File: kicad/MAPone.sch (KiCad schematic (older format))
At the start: 33 parts, among them J1 BARREL_JACK, J2 USB-Micro, P1 CONN_1, P2 CONN_1, P3 CONN_1, P4 CONN_1, SW1 RST, U1 7805, U2 ATMEGA328-P, X1 16MHz

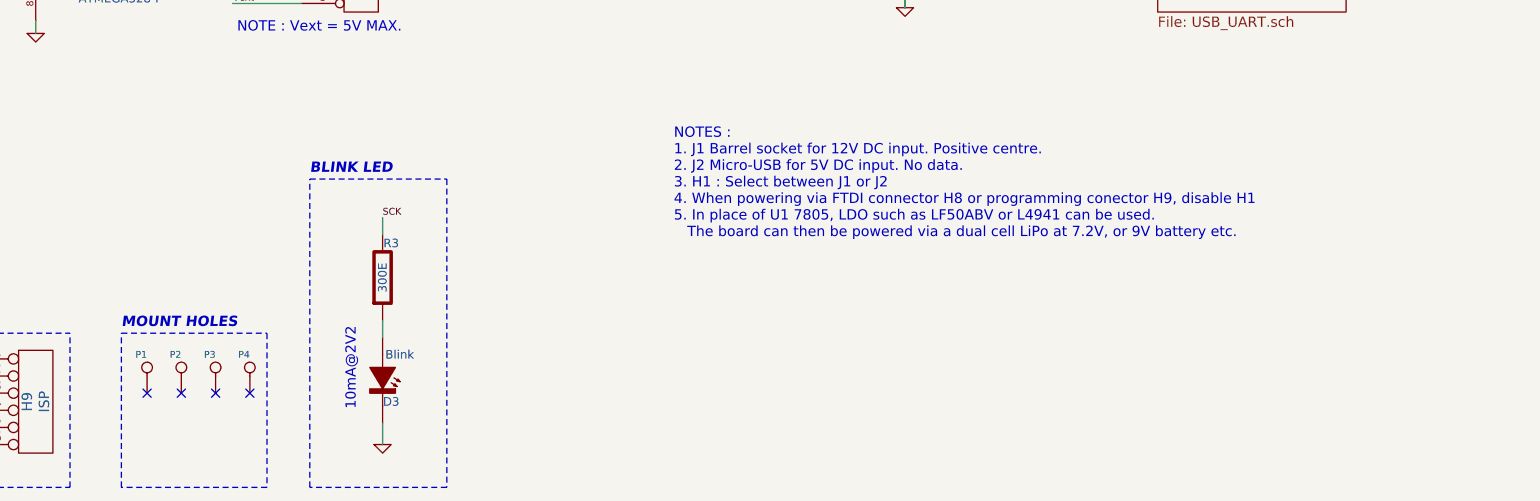
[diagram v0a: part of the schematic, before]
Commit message: MAPone Schematic, PCB, BoM complete. USB<>UART PCB work in progress
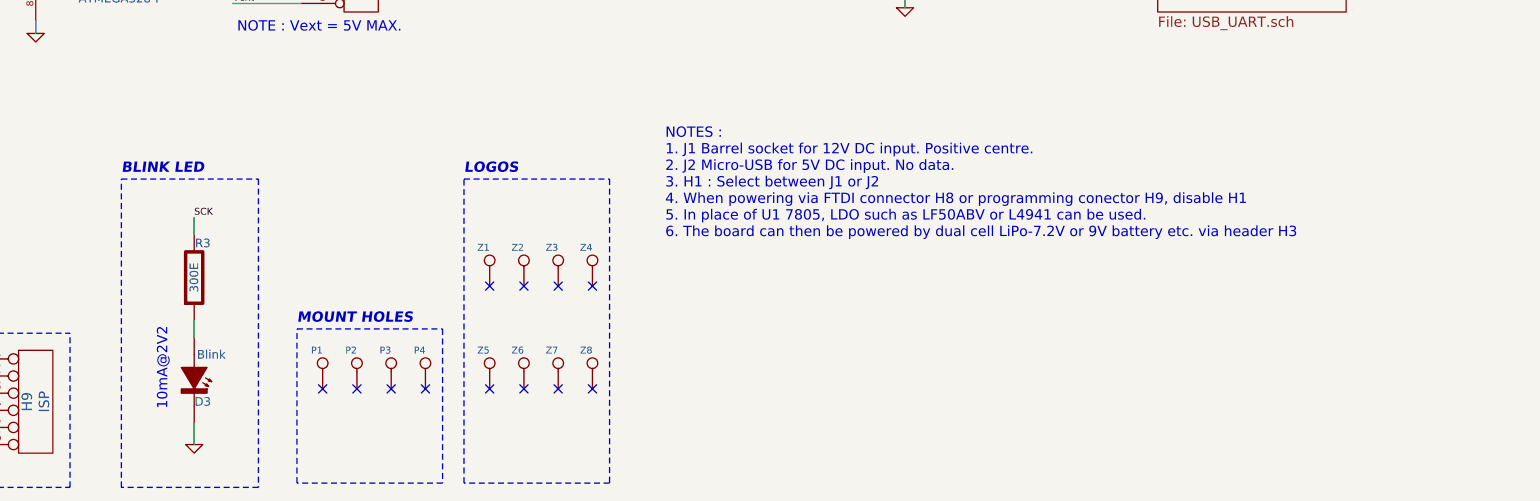
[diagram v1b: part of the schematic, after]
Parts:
- added Z1, Z2, Z3, Z4: CONN_1, MAPone.pretty:MA_Logo2, symbol CONN_1
- added Z5, Z6, Z7, Z8: CONN_1, MAPone:OSHW_6mm, symbol CONN_1
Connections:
- no-connect marks 10 -> 18
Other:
- note added: "LOGOS"
- note added: "NOTES :\n1. J1 Barrel socket for 12V DC input. Positive centre.\n2. J2 Micro-USB for 5V DC input. No data.\n3. H1 : Select between J1 or J2\n4. When powering via FTDI connector H8 or programming conector H9, disable H1\n5. In place of U1 7805, LDO such as LF50ABV or L4941 can be used. \n6. The board can then be powered by dual cell LiPo-7.2V or 9V battery etc. via header H3"
- note removed: "NOTES :\n1. J1 Barrel socket for 12V DC input. Positive centre.\n2. J2 Micro-USB for 5V DC input. No data.\n3. H1 : Select between J1 or J2\n4. When powering via FTDI connector H8 or programming conector H9, disable H1\n5. In place of U1 7805, LDO such as LF50ABV or L4941 can be used. \n The board can then be powered via a dual cell LiPo at 7.2V, or 9V battery etc."
- moved on the sheet: D3, P1, P2, P3, P4, R3
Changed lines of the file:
@@
 00 11 60 41 10 04 41 18 00 44 80 05 41 10 04 61 00 10 01 16 04 41 10 84 01 40 04 58 10 04 41 10
 06 00 11 60 41 10 04 41 18 00 44 80 05 41 10 04 61 00 10 01 16 04 41 10 84 01 E0 7F 01 2F 14 66
-D9 0D DF 91 84 00 00 00 00 49 45 4E 44 AE 42 60 82 48
+D9 0D DF 91 84 00 00 00 00 49 45 4E 44 AE 42 60 82 CE
 EndData
 $EndBitmap
@@
 Connection ~ 1325 2725
 Wire Wire Line
-	5300 7375 5300 7500
-Wire Wire Line
-	5300 6175 5300 6275
+	4200 7375 4200 7500
+Wire Wire Line
+	4200 6175 4200 6275
 Wire Wire Line
 	1050 2725 2375 2725
@@
 	1125 2625 1125 2500
 Wire Wire Line
-	5300 6775 5300 6875
+	4200 6775 4200 6875
 Wire Wire Line
 	10700 1350 10700 1550
@@
 $EndComp
 NoConn ~ 4575 1675
-Text Label 5300 6175 0    40   ~ 0
+Text Label 4200 6175 0    40   ~ 0
 SCK
 $Comp
 L GND #PWR03
 U 1 1 546B82E7
-P 5300 7500
-F 0 "#PWR03" H 5300 7500 30  0001 C CNN
-F 1 "GND" H 5300 7430 30  0001 C CNN
-F 2 "" H 5300 7500 60  0001 C CNN
-F 3 "" H 5300 7500 60  0001 C CNN
-	1    5300 7500
+P 4200 7500
+F 0 "#PWR03" H 4200 7500 30  0001 C CNN
+F 1 "GND" H 4200 7430 30  0001 C CNN
+F 2 "" H 4200 7500 60  0001 C CNN
+F 3 "" H 4200 7500 60  0001 C CNN
+	1    4200 7500
 	1    0    0    -1
 $EndComp
@@
 L R_CPL R3
 U 1 1 546B82ED
-P 5300 6525
-F 0 "R3" V 5100 6575 50  0000 C CNN
-F 1 "300E" H 5300 6525 50  0000 C CNN
-F 2 "MAPone.pretty:R_0805_HandSoldering" H 5300 6525 60  0001 C CNN
-F 3 "" H 5300 6525 60  0001 C CNN
-	1    5300 6525
+P 4200 6525
+F 0 "R3" V 4000 6575 50  0000 C CNN
+F 1 "300E" H 4200 6525 50  0000 C CNN
+F 2 "MAPone.pretty:R_0805_HandSoldering" H 4200 6525 60  0001 C CNN
+F 3 "" H 4200 6525 60  0001 C CNN
+	1    4200 6525
 	0    1    1    0
 $EndComp
@@
 L LED_CPL D3
 U 1 1 546B82F4
-P 5300 7125
-F 0 "D3" V 5425 7175 50  0000 C CNN
-F 1 "Blink" V 5150 7225 50  0000 C CNN
-F 2 "MAPone.pretty:LED-3MM" H 5300 7125 60  0001 C CNN
-F 3 "" H 5300 7125 60  0001 C CNN
-	1    5300 7125
+P 4200 7125
+F 0 "D3" V 4325 7175 50  0000 C CNN
+F 1 "Blink" V 4050 7225 50  0000 C CNN
+F 2 "MAPone.pretty:LED-3MM" H 4200 7125 60  0001 C CNN
+F 3 "" H 4200 7125 60  0001 C CNN
+	1    4200 7125
 	0    1    1    0
 $EndComp
@@
 L CONN_1 P2
 U 1 1 546B8348
-P 4125 7050
-F 0 "P2" V 4200 7050 40  0000 L CNN
-F 1 "CONN_1" H 4125 7105 30  0001 C CNN
-F 2 "MAPone.pretty:vite_3mm" H 4125 7050 60  0001 C CNN
-F 3 "" H 4125 7050 60  0001 C CNN
-	1    4125 7050
+P 5150 7025
+F 0 "P2" V 5225 7025 40  0000 L CNN
+F 1 "CONN_1" H 5150 7080 30  0001 C CNN
+F 2 "MAPone.pretty:vite_3mm" H 5150 7025 60  0001 C CNN
+F 3 "" H 5150 7025 60  0001 C CNN
+	1    5150 7025
 	0    -1   -1   0
 $EndComp
@@
 L CONN_1 P1
 U 1 1 546B834F
-P 3925 7050
-F 0 "P1" V 4000 7050 40  0000 L CNN
-F 1 "CONN_1" H 3925 7105 30  0001 C CNN
-F 2 "MAPone.pretty:vite_3mm" H 3925 7050 60  0001 C CNN
-F 3 "" H 3925 7050 60  0001 C CNN
-	1    3925 7050
+P 4950 7025
+F 0 "P1" V 5025 7025 40  0000 L CNN
+F 1 "CONN_1" H 4950 7080 30  0001 C CNN
+F 2 "MAPone.pretty:vite_3mm" H 4950 7025 60  0001 C CNN
+F 3 "" H 4950 7025 60  0001 C CNN
+	1    4950 7025
 	0    -1   -1   0
 $EndComp
@@
 $EndComp
 Wire Notes Line
-	4875 7750 4875 5950
-Wire Notes Line
-	4875 5950 5675 5950
-Wire Notes Line
-	5675 5950 5675 7750
-Wire Notes Line
-	5675 7750 4875 7750
-Text Notes 4875 5925 0    60   Italic 12
+	3775 7750 3775 5950
+Wire Notes Line
+	3775 5950 4575 5950
+Wire Notes Line
+	4575 5950 4575 7750
+Wire Notes Line
+	4575 7750 3775 7750
+Text Notes 3775 5925 0    60   Italic 12
 BLINK LED
 Wire Notes Line
-	3775 7750 3775 6850
-Wire Notes Line
-	3775 6850 4625 6850
-Wire Notes Line
-	4625 6850 4625 7750
-Wire Notes Line
-	4625 7750 3775 7750
-Text Notes 3775 6825 0    60   Italic 12
+	4800 7725 4800 6825
+Wire Notes Line
+	4800 6825 5650 6825
+Wire Notes Line
+	5650 6825 5650 7725
+Wire Notes Line
+	5650 7725 4800 7725
+Text Notes 4800 6800 0    60   Italic 12
 MOUNT HOLES
 $Comp
 L CONN_1 P3
 U 1 1 546F7776
-P 4325 7050
-F 0 "P3" V 4400 7050 40  0000 L CNN
-F 1 "CONN_1" H 4325 7105 30  0001 C CNN
-F 2 "MAPone.pretty:vite_3mm" H 4325 7050 60  0001 C CNN
-F 3 "" H 4325 7050 60  0001 C CNN
-	1    4325 7050
+P 5350 7025
+F 0 "P3" V 5425 7025 40  0000 L CNN
+F 1 "CONN_1" H 5350 7080 30  0001 C CNN
+F 2 "MAPone.pretty:vite_3mm" H 5350 7025 60  0001 C CNN
+F 3 "" H 5350 7025 60  0001 C CNN
+	1    5350 7025
 	0    -1   -1   0
 $EndComp
@@
 L CONN_1 P4
 U 1 1 546F77D2
-P 4525 7050
-F 0 "P4" V 4600 7050 40  0000 L CNN
-F 1 "CONN_1" H 4525 7105 30  0001 C CNN
-F 2 "MAPone.pretty:vite_3mm" H 4525 7050 60  0001 C CNN
-F 3 "" H 4525 7050 60  0001 C CNN
-	1    4525 7050
-	0    -1   -1   0
-$EndComp
-NoConn ~ 3925 7200
-NoConn ~ 4125 7200
-NoConn ~ 4325 7200
-NoConn ~ 4525 7200
+P 5550 7025
+F 0 "P4" V 5625 7025 40  0000 L CNN
+F 1 "CONN_1" H 5550 7080 30  0001 C CNN
+F 2 "MAPone.pretty:vite_3mm" H 5550 7025 60  0001 C CNN
+F 3 "" H 5550 7025 60  0001 C CNN
+	1    5550 7025
+	0    -1   -1   0
+$EndComp
+NoConn ~ 4950 7175
+NoConn ~ 5150 7175
+NoConn ~ 5350 7175
+NoConn ~ 5550 7175
 NoConn ~ 7225 1950
 NoConn ~ 7850 4175
@@
 Text Notes 4450 5100 0    60   ~ 0
 NOTE : Vext = 5V MAX.
-Text Notes 7000 6300 0    60   ~ 0
-NOTES :\n1. J1 Barrel socket for 12V DC input. Positive centre.\n2. J2 Micro-USB for 5V DC input. No data.\n3. H1 : Select between J1 or J2\n4. When powering via FTDI connector H8 or programming conector H9, disable H1\n5. In place of U1 7805, LDO such as LF50ABV or L4941 can be used. \n   The board can then be powered via a dual cell LiPo at 7.2V, or 9V battery etc.
+Text Notes 6950 6300 0    60   ~ 0
+NOTES :\n1. J1 Barrel socket for 12V DC input. Positive centre.\n2. J2 Micro-USB for 5V DC input. No data.\n3. H1 : Select between J1 or J2\n4. When powering via FTDI connector H8 or programming conector H9, disable H1\n5. In place of U1 7805, LDO such as LF50ABV or L4941 can be used. \n6. The board can then be powered by dual cell LiPo-7.2V or 9V battery etc. via header H3
 Text Notes 9850 2600 1    60   ~ 0
 10mA@2V
-Text Notes 5150 7300 1    60   ~ 0
+Text Notes 4050 7300 1    60   ~ 0
 10mA@2V2
 $Comp
@@
 F1 "USB_UART.sch" 60
 $EndSheet
+$Comp
+L CONN_1 Z6
+U 1 1 547C1C9E
+P 6125 7025
+F 0 "Z6" V 6200 7025 40  0000 L CNN
+F 1 "CONN_1" H 6125 7080 30  0001 C CNN
+F 2 "MAPone:OSHW_6mm" H 6125 7025 60  0001 C CNN
+F 3 "" H 6125 7025 60  0001 C CNN
+	1    6125 7025
+	0    -1   -1   0
+$EndComp
+$Comp
+L CONN_1 Z5
+U 1 1 547C1CA4
+P 5925 7025
+F 0 "Z5" V 6000 7025 40  0000 L CNN
+F 1 "CONN_1" H 5925 7080 30  0001 C CNN
+F 2 "MAPone:OSHW_6mm" H 5925 7025 60  0001 C CNN
+F 3 "" H 5925 7025 60  0001 C CNN
+	1    5925 7025
+	0    -1   -1   0
+$EndComp
+Wire Notes Line
+	5775 5950 6625 5950
+Wire Notes Line
+	6625 7725 5775 7725
+Text Notes 5775 5925 0    60   Italic 12
+LOGOS
+$Comp
+L CONN_1 Z7
+U 1 1 547C1CAF
+P 6325 7025
+F 0 "Z7" V 6400 7025 40  0000 L CNN
+F 1 "CONN_1" H 6325 7080 30  0001 C CNN
+F 2 "MAPone:OSHW_6mm" H 6325 7025 60  0001 C CNN
+F 3 "" H 6325 7025 60  0001 C CNN
+	1    6325 7025
+	0    -1   -1   0
+$EndComp
+$Comp
+L CONN_1 Z8
+U 1 1 547C1CB5
+P 6525 7025
+F 0 "Z8" V 6600 7025 40  0000 L CNN
+F 1 "CONN_1" H 6525 7080 30  0001 C CNN
+F 2 "MAPone:OSHW_6mm" H 6525 7025 60  0001 C CNN
+F 3 "" H 6525 7025 60  0001 C CNN
+	1    6525 7025
+	0    -1   -1   0
+$EndComp
+NoConn ~ 5925 7175
+NoConn ~ 6125 7175
+NoConn ~ 6325 7175
+NoConn ~ 6525 7175
+Wire Notes Line
+	5775 7725 5775 5950
+Wire Notes Line
+	6625 5950 6625 7725
+$Comp
+L CONN_1 Z2
+U 1 1 547C2244
+P 6125 6425
+F 0 "Z2" V 6200 6425 40  0000 L CNN
+F 1 "CONN_1" H 6125 6480 30  0001 C CNN
+F 2 "MAPone.pretty:MA_Logo2" H 6125 6425 60  0001 C CNN
+F 3 "" H 6125 6425 60  0001 C CNN
+	1    6125 6425
+	0    -1   -1   0
+$EndComp
+$Comp
+L CONN_1 Z1
+U 1 1 547C224A
+P 5925 6425
+F 0 "Z1" V 6000 6425 40  0000 L CNN
+F 1 "CONN_1" H 5925 6480 30  0001 C CNN
+F 2 "MAPone.pretty:MA_Logo2" H 5925 6425 60  0001 C CNN
+F 3 "" H 5925 6425 60  0001 C CNN
+	1    5925 6425
+	0    -1   -1   0
+$EndComp
+$Comp
+L CONN_1 Z3
+U 1 1 547C2250
+P 6325 6425
+F 0 "Z3" V 6400 6425 40  0000 L CNN
+F 1 "CONN_1" H 6325 6480 30  0001 C CNN
+F 2 "MAPone.pretty:MA_Logo2" H 6325 6425 60  0001 C CNN
+F 3 "" H 6325 6425 60  0001 C CNN
+	1    6325 6425
+	0    -1   -1   0
+$EndComp
+$Comp
+L CONN_1 Z4
+U 1 1 547C2256
+P 6525 6425
+F 0 "Z4" V 6600 6425 40  0000 L CNN
+F 1 "CONN_1" H 6525 6480 30  0001 C CNN
+F 2 "MAPone.pretty:MA_Logo2" H 6525 6425 60  0001 C CNN
+F 3 "" H 6525 6425 60  0001 C CNN
+	1    6525 6425
+	0    -1   -1   0
+$EndComp
+NoConn ~ 5925 6575
+NoConn ~ 6125 6575
+NoConn ~ 6325 6575
+NoConn ~ 6525 6575
 $EndSCHEMATC

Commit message: MAPone USB<>USART complete. preliminary gerbers generated
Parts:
- removed Z4: CONN_1, MAPone.pretty:MA_Logo2, symbol CONN_1
- removed Z8: CONN_1, MAPone:OSHW_6mm, symbol CONN_1
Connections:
- net 5V: now also H3.2 (PM); no longer H3.1 (P1)
- net GND: now also H3.1 (P1); no longer H3.2 (PM)
- no-connect marks 18 -> 16
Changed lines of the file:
@@
 00 11 60 41 10 04 41 18 00 44 80 05 41 10 04 61 00 10 01 16 04 41 10 84 01 40 04 58 10 04 41 10
 06 00 11 60 41 10 04 41 18 00 44 80 05 41 10 04 61 00 10 01 16 04 41 10 84 01 E0 7F 01 2F 14 66
-D9 0D DF 91 84 00 00 00 00 49 45 4E 44 AE 42 60 82 CE
+D9 0D DF 91 84 00 00 00 00 49 45 4E 44 AE 42 60 82 6C
 EndData
 $EndBitmap
@@
 F 3 "" H 10900 2100 60  0000 C CNN
 	1    10900 2100
-	1    0    0    -1
+	1    0    0    1
 $EndComp
 Wire Wire Line
@@
 	0    -1   -1   0
 $EndComp
-$Comp
-L CONN_1 Z8
-U 1 1 547C1CB5
-P 6525 7025
-F 0 "Z8" V 6600 7025 40  0000 L CNN
-F 1 "CONN_1" H 6525 7080 30  0001 C CNN
-F 2 "MAPone:OSHW_6mm" H 6525 7025 60  0001 C CNN
-F 3 "" H 6525 7025 60  0001 C CNN
-	1    6525 7025
-	0    -1   -1   0
-$EndComp
 NoConn ~ 5925 7175
 NoConn ~ 6125 7175
 NoConn ~ 6325 7175
-NoConn ~ 6525 7175
 Wire Notes Line
 	5775 7725 5775 5950
@@
 	0    -1   -1   0
 $EndComp
-$Comp
-L CONN_1 Z4
-U 1 1 547C2256
-P 6525 6425
-F 0 "Z4" V 6600 6425 40  0000 L CNN
-F 1 "CONN_1" H 6525 6480 30  0001 C CNN
-F 2 "MAPone.pretty:MA_Logo2" H 6525 6425 60  0001 C CNN
-F 3 "" H 6525 6425 60  0001 C CNN
-	1    6525 6425
-	0    -1   -1   0
-$EndComp
 NoConn ~ 5925 6575
 NoConn ~ 6125 6575
 NoConn ~ 6325 6575
-NoConn ~ 6525 6575
 $EndSCHEMATC

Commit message: MAPone realigned headers to fit 0.1 breadboard
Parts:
- Z1, Z2, Z3, Z5, Z6, Z7: symbol CONN_1 -> SCREW
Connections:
- net 3V3: now also H2.5; no longer H2.2
- net 5V: now also H2.4; no longer H2.3
- net AD0: now also H4.6; no longer H4.1
- net AD1: now also H4.5; no longer H4.2
- net AD2: now also H4.4; no longer H4.3
- net AD3: now also H4.3; no longer H4.4
- net AD4_SDA: now also H4.2; no longer H4.5
- net AD5_SCL: now also H4.1; no longer H4.6
- net GND: now also H2.2, H2.3; no longer H2.4, H2.5
- net RST: now also H2.6; no longer H2.1
- net V_IN: now also H2.1; no longer H2.6
- no-connect marks 16 -> 10

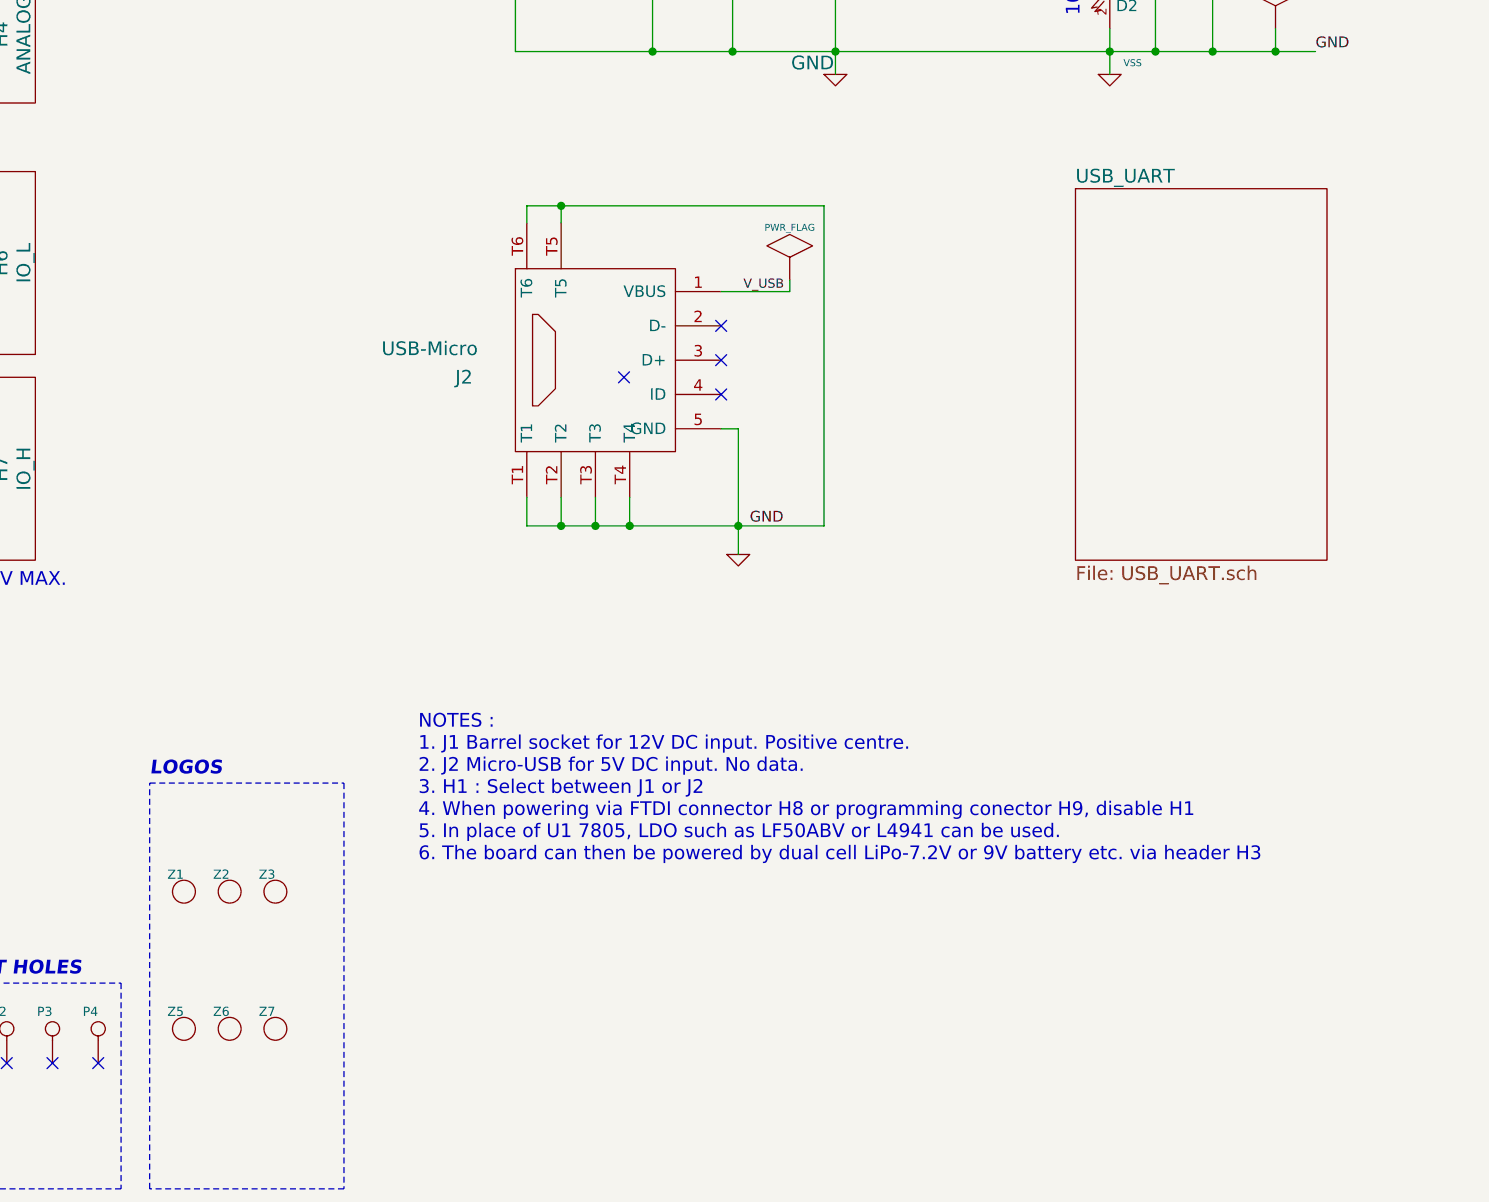
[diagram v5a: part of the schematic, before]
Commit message: MAPone hived off USB<>UART bridge to separate project MAPusart
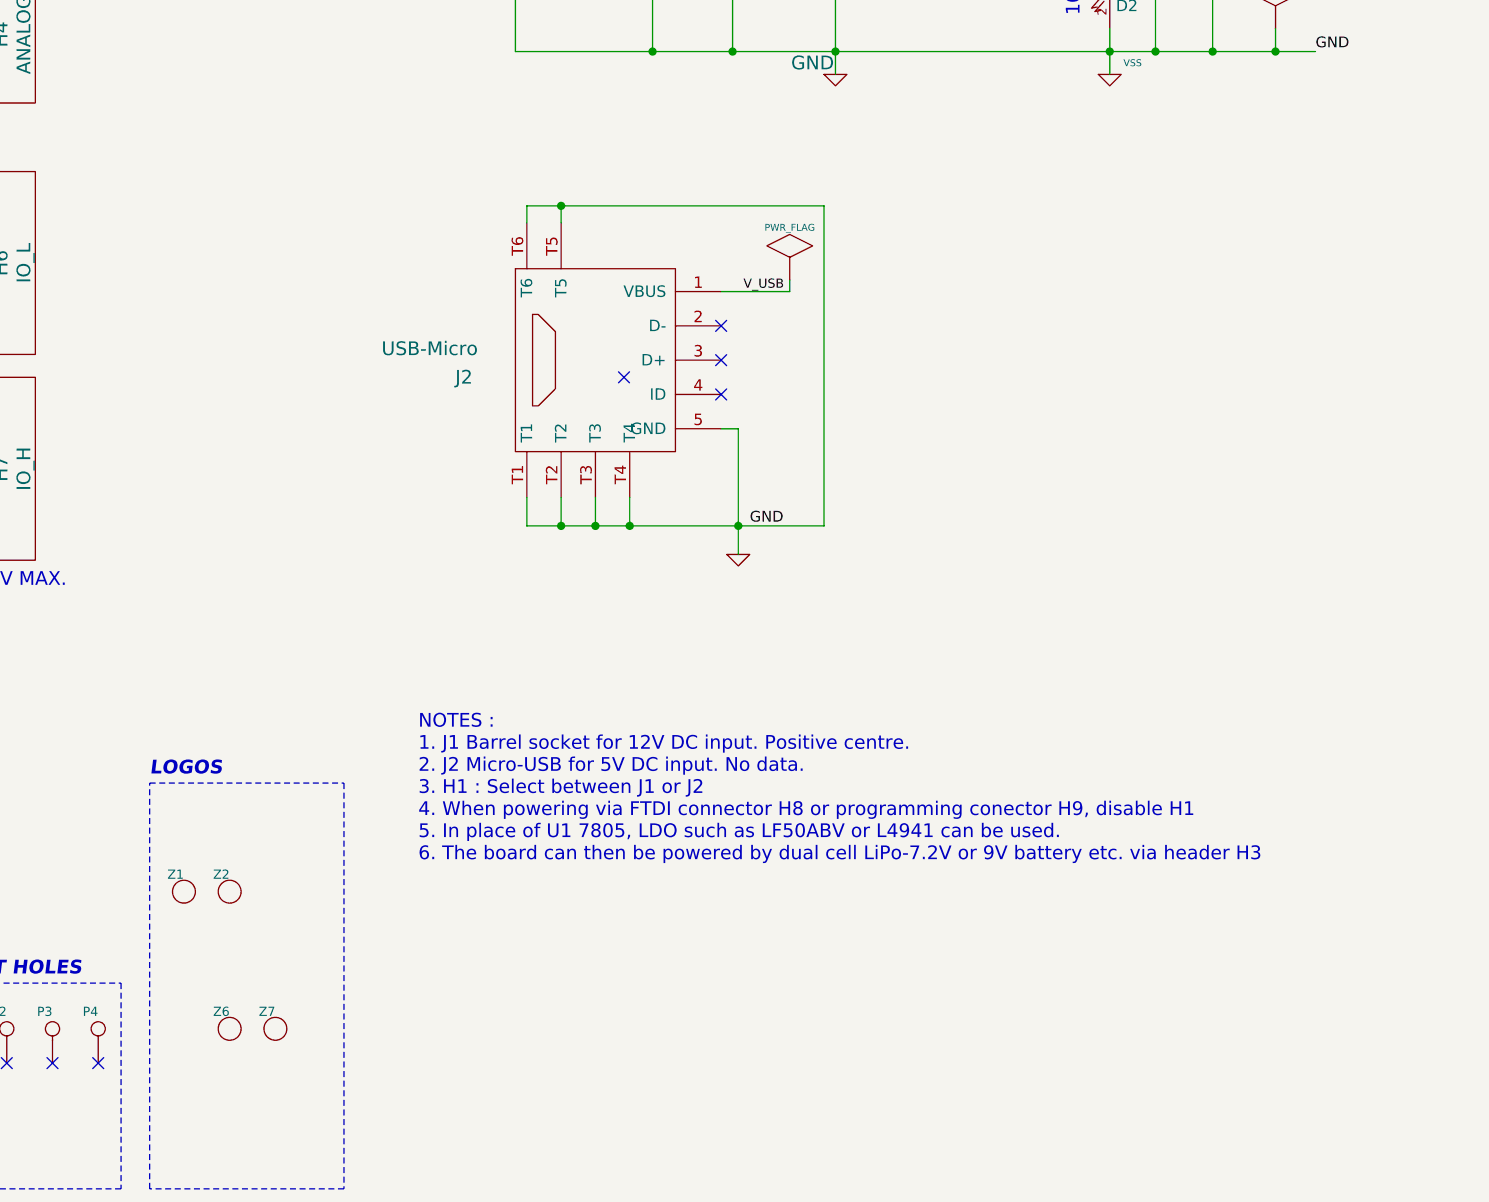
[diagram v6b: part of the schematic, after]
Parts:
- removed Z3: CONN_1, MAPone.pretty:MA_Logo2, symbol SCREW
- removed Z5: CONN_1, MAPone:OSHW_6mm, symbol SCREW
